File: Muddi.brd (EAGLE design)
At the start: 106.3 x 95.2 mm, 16 parts, among them IC1 7805TV, J1 DCJ0202

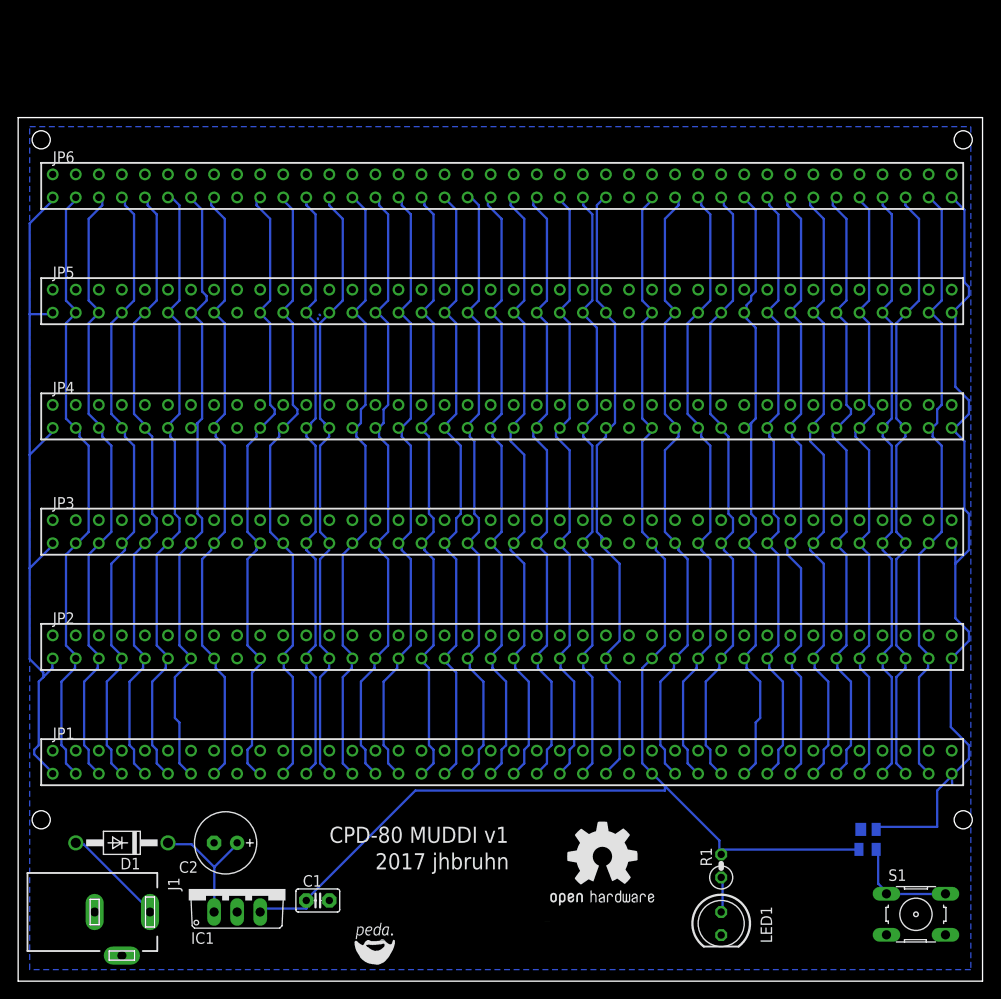
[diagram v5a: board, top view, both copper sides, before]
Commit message: Add more Texts
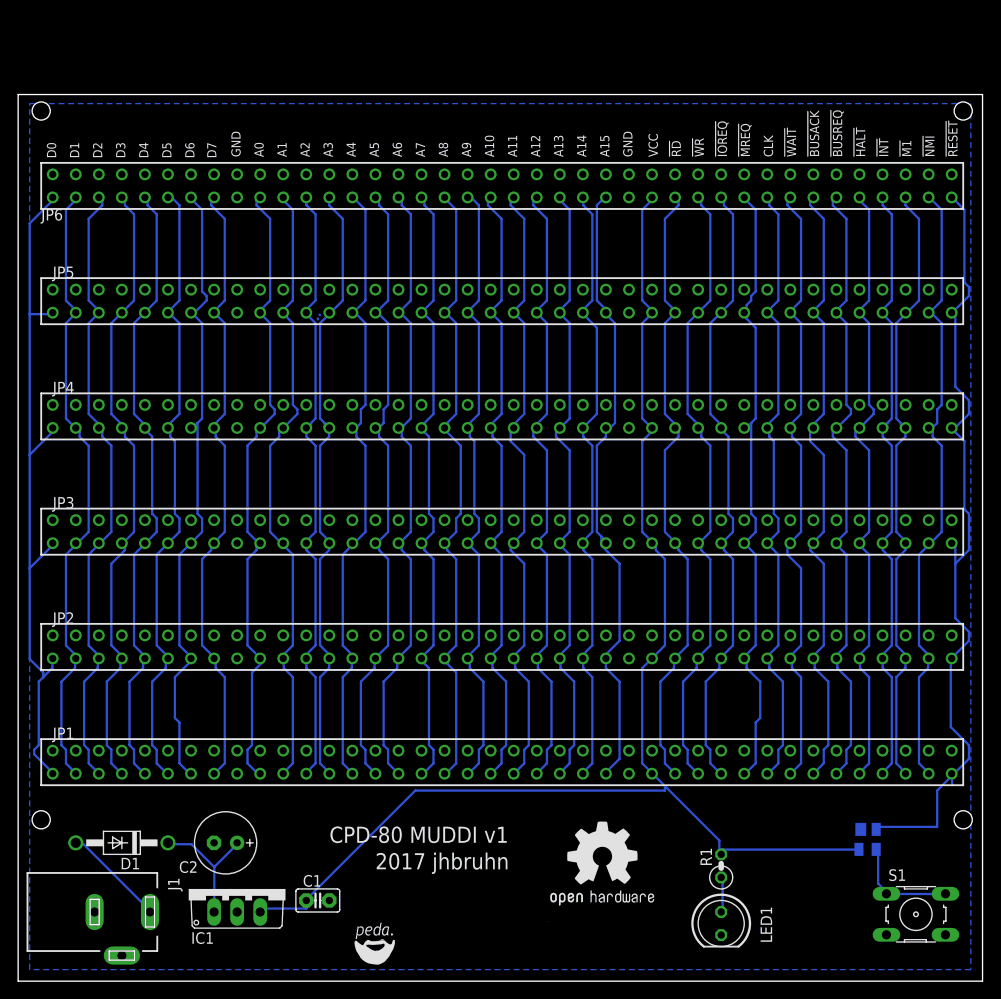
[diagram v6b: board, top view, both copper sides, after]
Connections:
- net N$1 renamed D0
- net N$24 renamed A15
- net N$37 renamed !BUSACK
- net N$38 renamed !BUSREQ
- net N$39 renamed !M1
- net N$40 renamed !RESE
- net N$41 renamed !HALT
- net N$42 renamed !NMI
- net N$43 renamed !INT
- net N$44 renamed CLK
- net N$45 renamed !MREQ
- net N$46 renamed !IOREQ
- net N$47 renamed !WAIT
- net N$48 renamed !RD
- net N$49 renamed !WR
- net N$8 renamed D7
- net N$9 renamed A0
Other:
- board size 106.3 x 95.2 mm -> 106.3 x 97.7 mm
- board text added: "!BUSACK"
- board text added: "!BUSREQ"
- board text added: "!HALT"
- board text added: "!INT"
- board text added: "!IOREQ"
- board text added: "!M1"
- board text added: "!MREQ"
- board text added: "!NMI"
- board text added: "!RD"
- board text added: "!RESET"
- board text added: "!WAIT"
- board text added: "!WR"
- board text added: "A0"
- board text added: "A1"
- board text added: "A10"
- board text added: "A11"
- board text added: "A12"
- board text added: "A13"
- board text added: "A14"
- board text added: "A15"
- board text added: "A2"
- board text added: "A3"
- board text added: "A4"
- board text added: "A5"
- board text added: "A6"
- board text added: "A7"
- board text added: "A8"
- board text added: "A9"
- board text added: "CLK"
- board text added: "D0"
- board text added: "D1"
- board text added: "D2"
- board text added: "D3"
- board text added: "D4"
- board text added: "D5"
- board text added: "D6"
- board text added: "D7"
- board text added: "GND"
- board text added: "VCC"
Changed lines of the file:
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@@
 <setting verticaltext="up"/>
 </settings>
-<grid distance="0.05" unitdist="inch" unit="mm" style="lines" multiple="1" display="no" altdistance="0.005" altunitdist="inch" altunit="mm"/>
+<grid distance="0.05" unitdist="inch" unit="mm" style="lines" multiple="1" display="no" altdistance="0.635" altunitdist="mm" altunit="mm"/>
 <layers>
 <layer number="1" name="Top" color="4" fill="1" visible="yes" active="yes"/>
@@
 <plain>
 <wire x1="-1.27" y1="0" x2="105" y2="0" width="0" layer="20"/>
-<wire x1="105" y1="0" x2="105" y2="95.16" width="0" layer="20"/>
-<wire x1="105" y1="95.16" x2="-1.27" y2="95.16" width="0" layer="20"/>
-<wire x1="-1.27" y1="95.16" x2="-1.27" y2="0" width="0" layer="20"/>
+<wire x1="105" y1="0" x2="105" y2="97.7" width="0" layer="20"/>
+<wire x1="105" y1="97.7" x2="-1.27" y2="97.7" width="0" layer="20"/>
+<wire x1="-1.27" y1="97.7" x2="-1.27" y2="0" width="0" layer="20"/>
 <text x="33.02" y="15.24" size="1.778" layer="21" font="fixed">CPD-80 MUDDI v1</text>
 <rectangle x1="38.1381" y1="1.8161" x2="38.4683" y2="1.8415" layer="21"/>
@@
 <hole x="1.27" y="17.78" drill="2"/>
 <hole x="102.87" y="17.78" drill="2"/>
-<hole x="1.27" y="92.71" drill="2"/>
-<hole x="102.87" y="92.71" drill="2"/>
+<hole x="1.27" y="95.885" drill="2"/>
+<hole x="102.87" y="95.885" drill="2"/>
+<text x="2.921" y="90.678" size="1.016" layer="21" font="fixed" rot="R90">D0</text>
+<text x="20.574" y="90.678" size="1.016" layer="21" font="fixed" rot="R90">D7</text>
+<text x="25.781" y="90.805" size="1.016" layer="21" font="fixed" rot="R90">A0</text>
+<text x="23.241" y="90.805" size="1.016" layer="21" font="fixed" rot="R90">GND</text>
+<text x="63.881" y="90.805" size="1.016" layer="21" font="fixed" rot="R90">A15</text>
+<text x="66.421" y="90.805" size="1.016" layer="21" font="fixed" rot="R90">GND</text>
+<text x="69.215" y="90.805" size="1.016" layer="21" font="fixed" rot="R90">VCC</text>
+<text x="71.755" y="90.805" size="1.016" layer="21" font="fixed" rot="R90">!RD</text>
+<text x="74.295" y="90.805" size="1.016" layer="21" font="fixed" rot="R90">!WR</text>
+<text x="76.835" y="90.805" size="1.016" layer="21" font="fixed" rot="R90">!IOREQ</text>
+<text x="79.375" y="90.805" size="1.016" layer="21" font="fixed" rot="R90">!MREQ</text>
+<text x="81.915" y="90.805" size="1.016" layer="21" font="fixed" rot="R90">CLK</text>
+<text x="84.455" y="90.805" size="1.016" layer="21" font="fixed" rot="R90">!WAIT</text>
+<text x="86.995" y="90.805" size="1.016" layer="21" font="fixed" rot="R90">!BUSACK</text>
+<text x="89.535" y="90.805" size="1.016" layer="21" font="fixed" rot="R90">!BUSREQ</text>
+<text x="92.075" y="90.805" size="1.016" layer="21" font="fixed" rot="R90">!HALT</text>
+<text x="94.615" y="90.805" size="1.016" layer="21" font="fixed" rot="R90">!INT</text>
+<text x="97.155" y="90.805" size="1.016" layer="21" font="fixed" rot="R90">!M1</text>
+<text x="99.695" y="90.805" size="1.016" layer="21" font="fixed" rot="R90">!NMI</text>
+<text x="102.235" y="90.805" size="1.016" layer="21" font="fixed" rot="R90">!RESET</text>
+<text x="5.461" y="90.678" size="1.016" layer="21" font="fixed" rot="R90">D1</text>
+<text x="8.001" y="90.678" size="1.016" layer="21" font="fixed" rot="R90">D2</text>
+<text x="10.541" y="90.678" size="1.016" layer="21" font="fixed" rot="R90">D3</text>
+<text x="13.081" y="90.678" size="1.016" layer="21" font="fixed" rot="R90">D4</text>
+<text x="15.621" y="90.678" size="1.016" layer="21" font="fixed" rot="R90">D5</text>
+<text x="18.161" y="90.678" size="1.016" layer="21" font="fixed" rot="R90">D6</text>
+<text x="28.321" y="90.805" size="1.016" layer="21" font="fixed" rot="R90">A1</text>
+<text x="30.861" y="90.805" size="1.016" layer="21" font="fixed" rot="R90">A2</text>
+<text x="33.401" y="90.805" size="1.016" layer="21" font="fixed" rot="R90">A3</text>
+<text x="35.941" y="90.805" size="1.016" layer="21" font="fixed" rot="R90">A4</text>
+<text x="38.481" y="90.805" size="1.016" layer="21" font="fixed" rot="R90">A5</text>
+<text x="41.021" y="90.805" size="1.016" layer="21" font="fixed" rot="R90">A6</text>
+<text x="43.561" y="90.805" size="1.016" layer="21" font="fixed" rot="R90">A7</text>
+<text x="46.101" y="90.805" size="1.016" layer="21" font="fixed" rot="R90">A8</text>
+<text x="48.641" y="90.805" size="1.016" layer="21" font="fixed" rot="R90">A9</text>
+<text x="51.181" y="90.805" size="1.016" layer="21" font="fixed" rot="R90">A10</text>
+<text x="53.721" y="90.805" size="1.016" layer="21" font="fixed" rot="R90">A11</text>
+<text x="56.261" y="90.805" size="1.016" layer="21" font="fixed" rot="R90">A12</text>
+<text x="58.801" y="90.805" size="1.016" layer="21" font="fixed" rot="R90">A13</text>
+<text x="61.341" y="90.805" size="1.016" layer="21" font="fixed" rot="R90">A14</text>
 </plain>
 <attributes>
@@
 <element name="JP4" library="jean" package="57102-F08-25" value="" x="11.43" y="62.23"/>
 <element name="JP5" library="jean" package="57102-F08-25" value="" x="11.43" y="74.93"/>
-<element name="JP6" library="jean" package="57102-F08-25" value="" x="11.43" y="87.63"/>
+<element name="JP6" library="jean" package="57102-F08-25" value="" x="11.43" y="87.63" smashed="yes">
+<attribute name="NAME" x="1.27" y="83.82" size="1.27" layer="25"/>
+<attribute name="VALUE" x="2.54" y="83.185" size="1.27" layer="27"/>
+</element>
 <element name="S1" library="switch-omron" package="B3F-10XX" value="RESET" x="97.663" y="7.366">
 <attribute name="OC_FARNELL" value="176432" x="97.663" y="7.366" size="1.778" layer="27" display="off"/>
@@
 </elements>
 <signals>
-<signal name="N$1">
+<signal name="D0">
 <contactref element="JP1" pad="1"/>
 <contactref element="JP2" pad="1"/>
@@
 <wire x1="18" y1="48.5" x2="17.78" y2="48.26" width="0.254" layer="16"/>
 </signal>
-<signal name="N$8">
+<signal name="D7">
 <contactref element="JP6" pad="15"/>
 <contactref element="JP5" pad="15"/>
@@
 <wire x1="20.5" y1="61" x2="20.32" y2="60.96" width="0.254" layer="16"/>
 </signal>
-<signal name="N$9">
+<signal name="A0">
 <contactref element="JP1" pad="19"/>
 <contactref element="JP2" pad="19"/>
@@
 <wire x1="61" y1="73.5" x2="60.96" y2="73.66" width="0.254" layer="16"/>
 </signal>
-<signal name="N$24">
+<signal name="A15">
 <contactref element="JP2" pad="49"/>
 <contactref element="JP1" pad="49"/>
@@
 <wire x1="63.5" y1="60.5" x2="63.5" y2="60.96" width="0.254" layer="16"/>
 </signal>
-<signal name="N$37">
+<signal name="!BUSACK">
 <contactref element="JP2" pad="67"/>
 <contactref element="JP1" pad="67"/>
@@
 <wire x1="86.5" y1="61" x2="86.36" y2="60.96" width="0.254" layer="16"/>
 </signal>
-<signal name="N$38">
+<signal name="!BUSREQ">
 <contactref element="JP1" pad="69"/>
 <contactref element="JP2" pad="69"/>
@@
 <wire x1="89" y1="61" x2="88.9" y2="60.96" width="0.254" layer="16"/>
 </signal>
-<signal name="N$39">
+<signal name="!M1">
 <contactref element="JP2" pad="75"/>
 <contactref element="JP1" pad="75"/>
@@
 <wire x1="96.5" y1="60.5" x2="96.52" y2="60.96" width="0.254" layer="16"/>
 </signal>
-<signal name="N$40">
+<signal name="!RESE">
 <contactref element="JP1" pad="79"/>
 <contactref element="JP2" pad="79"/>
@@
 <wire x1="102" y1="60.5" x2="101.6" y2="60.96" width="0.254" layer="16"/>
 </signal>
-<signal name="N$41">
+<signal name="!HALT">
 <contactref element="JP2" pad="71"/>
 <contactref element="JP1" pad="71"/>
@@
 <wire x1="91.5" y1="61" x2="91.44" y2="60.96" width="0.254" layer="16"/>
 </signal>
-<signal name="N$42">
+<signal name="!NMI">
 <contactref element="JP1" pad="77"/>
 <contactref element="JP2" pad="77"/>
@@
 <wire x1="99.5" y1="61" x2="99.06" y2="60.96" width="0.254" layer="16"/>
 </signal>
-<signal name="N$43">
+<signal name="!INT">
 <contactref element="JP2" pad="73"/>
 <contactref element="JP1" pad="73"/>
@@
 <wire x1="94" y1="60.5" x2="93.98" y2="60.96" width="0.254" layer="16"/>
 </signal>
-<signal name="N$44">
+<signal name="CLK">
 <contactref element="JP1" pad="63"/>
 <contactref element="JP2" pad="63"/>
@@
 <wire x1="81.5" y1="61" x2="81.28" y2="60.96" width="0.254" layer="16"/>
 </signal>
-<signal name="N$45">
+<signal name="!MREQ">
 <contactref element="JP2" pad="61"/>
 <contactref element="JP1" pad="61"/>
@@
 <wire x1="79" y1="48.5" x2="78.74" y2="48.26" width="0.254" layer="16"/>
 </signal>
-<signal name="N$46">
+<signal name="!IOREQ">
 <contactref element="JP1" pad="59"/>
 <contactref element="JP2" pad="59"/>
@@
 <wire x1="76" y1="61" x2="76.2" y2="60.96" width="0.254" layer="16"/>
 </signal>
-<signal name="N$47">
+<signal name="!WAIT">
 <contactref element="JP2" pad="65"/>
 <contactref element="JP1" pad="65"/>
@@
 <wire x1="84" y1="61" x2="83.82" y2="60.96" width="0.254" layer="16"/>
 </signal>
-<signal name="N$48">
+<signal name="!RD">
 <contactref element="JP1" pad="55"/>
 <contactref element="JP2" pad="55"/>
@@
 <wire x1="71" y1="61" x2="71.12" y2="60.96" width="0.254" layer="16"/>
 </signal>
-<signal name="N$49">
+<signal name="!WR">
 <contactref element="JP2" pad="57"/>
 <contactref element="JP1" pad="57"/>
@@
 <contactref element="JP6" pad="51"/>
 <polygon width="0.254" layer="16" isolate="0.3048">
-<vertex x="0" y="94.16"/>
-<vertex x="103.7082" y="94.16"/>
+<vertex x="0" y="96.7"/>
+<vertex x="103.7082" y="96.7"/>
 <vertex x="103.7082" y="1.27"/>
 <vertex x="0" y="1.27"/>

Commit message: Fix stupid VCC/GND mistakes on Address decoder
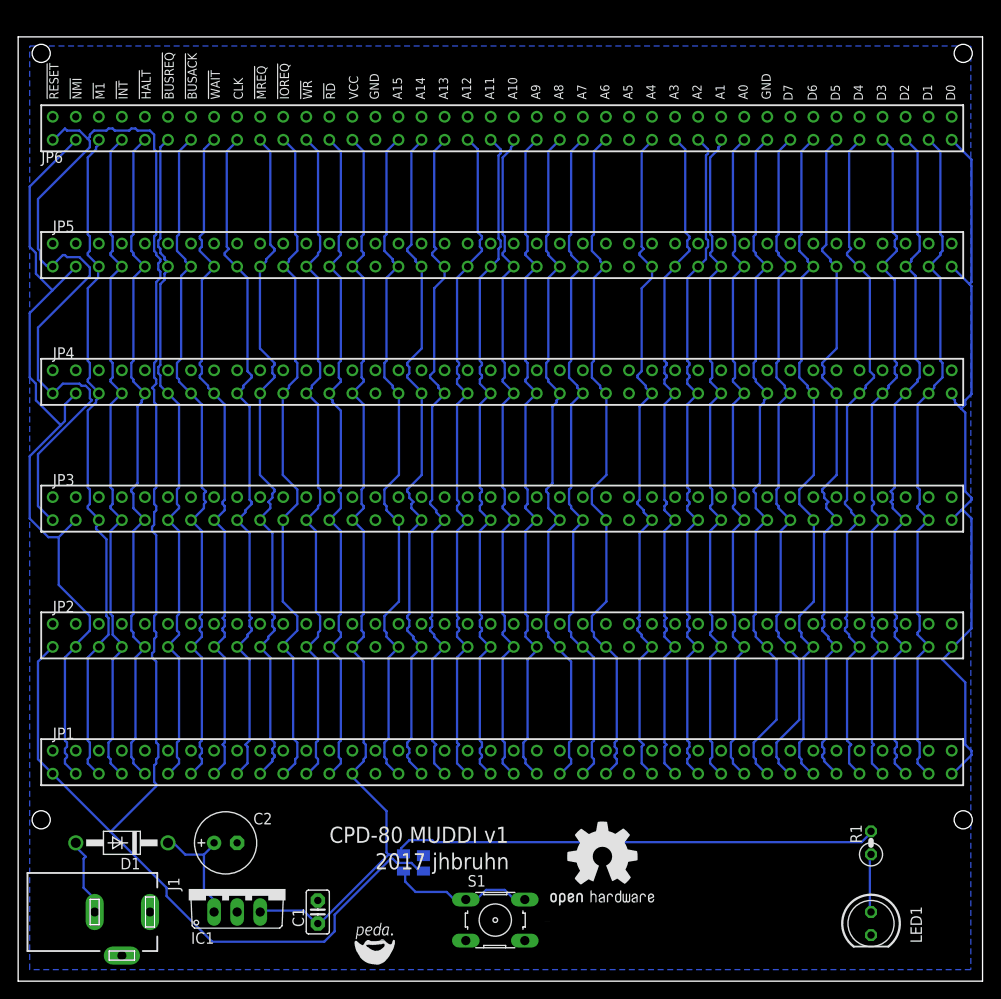
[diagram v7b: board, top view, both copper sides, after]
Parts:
- moved MAX811 50.1 mm to (42.3, 13.1), turned to 270 degrees
- moved S1 46.4 mm to (51.3, 6.73)
- moved R1 16.7 mm to (92.7, 15.2)
- moved LED1 16.5 mm to (92.7, 6.35)
- moved JP6 6.35 mm to (11.4, 94.0)
- moved JP5 5.08 mm to (11.4, 80.0)
- moved JP4 3.81 mm to (11.4, 66.0)
- moved JP3 2.54 mm to (11.4, 52.1)
- moved JP2 1.27 mm to (11.4, 38.1)
- moved C1 1.27 mm to (31.8, 7.62), turned to 90 degrees
- turned C2 to 0 degrees
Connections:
- removed net N$28: D1.A, J1.1
- new net N$1: D1.A, J1.3
- net !BUSACK: now also JP1.13, JP2.13, JP3.13, JP4.13, JP5.13, JP6.13; no longer JP1.67, JP2.67, JP3.67, JP4.67, JP5.67, JP6.67
- net !BUSREQ: now also JP1.11, JP2.11, JP3.11, JP4.11, JP5.11, JP6.11; no longer JP1.69, JP2.69, JP3.69, JP4.69, JP5.69, JP6.69
- net !HALT: now also JP1.9, JP2.9, JP3.9, JP4.9, JP5.9, JP6.9; no longer JP1.71, JP2.71, JP3.71, JP4.71, JP5.71, JP6.71
- net !INT: now also JP1.7, JP2.7, JP3.7, JP4.7, JP5.7, JP6.7; no longer JP1.73, JP2.73, JP3.73, JP4.73, JP5.73, JP6.73
- net !IOREQ: now also JP1.21, JP2.21, JP3.21, JP4.21, JP5.21, JP6.21; no longer JP1.59, JP2.59, JP3.59, JP4.59, JP5.59, JP6.59
- net !M1: now also JP1.5, JP2.5, JP3.5, JP4.5, JP5.5, JP6.5; no longer JP1.75, JP2.75, JP3.75, JP4.75, JP5.75, JP6.75
- net !MREQ: now also JP1.19, JP2.19, JP3.19, JP4.19, JP5.19, JP6.19; no longer JP1.61, JP2.61, JP3.61, JP4.61, JP5.61, JP6.61
- net !NMI: now also JP1.3, JP2.3, JP3.3, JP4.3, JP5.3, JP6.3; no longer JP1.77, JP2.77, JP3.77, JP4.77, JP5.77, JP6.77
- net !RD: now also JP1.25, JP2.25, JP3.25, JP4.25, JP5.25, JP6.25; no longer JP1.55, JP2.55, JP3.55, JP4.55, JP5.55, JP6.55
- net !RESE: now also JP1.1, JP2.1, JP3.1, JP4.1, JP5.1, JP6.1; no longer JP1.79, JP2.79, JP3.79, JP4.79, JP5.79, JP6.79
- net !WAIT: now also JP1.15, JP2.15, JP3.15, JP4.15, JP5.15, JP6.15; no longer JP1.65, JP2.65, JP3.65, JP4.65, JP5.65, JP6.65
- net !WR: now also JP1.23, JP2.23, JP3.23, JP4.23, JP5.23, JP6.23; no longer JP1.57, JP2.57, JP3.57, JP4.57, JP5.57, JP6.57
- net A0: now also JP1.63, JP2.63, JP3.63, JP4.63, JP5.63, JP6.63; no longer JP1.19, JP2.19, JP3.19, JP4.19, JP5.19, JP6.19
- net A15: now also JP1.31, JP2.31, JP3.31, JP4.31, JP5.31, JP6.31; no longer JP1.49, JP2.49, JP3.49, JP4.49, JP5.49, JP6.49
- net CLK: now also JP1.17, JP2.17, JP3.17, JP4.17, JP5.17, JP6.17; no longer JP1.63, JP2.63, JP3.63, JP4.63, JP5.63, JP6.63
- net D0: now also JP1.79, JP2.79, JP3.79, JP4.79, JP5.79, JP6.79; no longer JP1.1, JP2.1, JP3.1, JP4.1, JP5.1, JP6.1
- net D7: now also JP1.65, JP2.65, JP3.65, JP4.65, JP5.65, JP6.65; no longer JP1.15, JP2.15, JP3.15, JP4.15, JP5.15, JP6.15
- net GND: now also J1.1, JP1.29, JP2.29, JP3.29, JP4.29, JP5.29, JP6.29; no longer J1.3, JP1.17, JP2.17, JP3.17, JP4.17, JP5.17, JP6.17
- net N$10: now also JP1.61, JP2.61, JP3.61, JP4.61, JP5.61, JP6.61; no longer JP1.21, JP2.21, JP3.21, JP4.21, JP5.21, JP6.21
- net N$11: now also JP1.59, JP2.59, JP3.59, JP4.59, JP5.59, JP6.59; no longer JP1.23, JP2.23, JP3.23, JP4.23, JP5.23, JP6.23
- net N$12: now also JP1.57, JP2.57, JP3.57, JP4.57, JP5.57, JP6.57; no longer JP1.25, JP2.25, JP3.25, JP4.25, JP5.25, JP6.25
- net N$13: now also JP1.55, JP2.55, JP3.55, JP4.55, JP5.55, JP6.55; no longer JP1.27, JP2.27, JP3.27, JP4.27, JP5.27, JP6.27
- net N$14: now also JP1.53, JP2.53, JP3.53, JP4.53, JP5.53, JP6.53; no longer JP1.29, JP2.29, JP3.29, JP4.29, JP5.29, JP6.29
- net N$15: now also JP1.49, JP2.49, JP3.49, JP4.49, JP5.49, JP6.49; no longer JP1.31, JP2.31, JP3.31, JP4.31, JP5.31, JP6.31
- net N$2: now also JP1.77, JP2.77, JP3.77, JP4.77, JP5.77, JP6.77; no longer JP1.3, JP2.3, JP3.3, JP4.3, JP5.3, JP6.3
- net N$3: now also JP1.75, JP2.75, JP3.75, JP4.75, JP5.75, JP6.75; no longer JP1.5, JP2.5, JP3.5, JP4.5, JP5.5, JP6.5
- net N$4: now also JP1.73, JP2.73, JP3.73, JP4.73, JP5.73, JP6.73; no longer JP1.7, JP2.7, JP3.7, JP4.7, JP5.7, JP6.7
- net N$5: now also JP1.71, JP2.71, JP3.71, JP4.71, JP5.71, JP6.71; no longer JP1.9, JP2.9, JP3.9, JP4.9, JP5.9, JP6.9
- net N$6: now also JP1.69, JP2.69, JP3.69, JP4.69, JP5.69, JP6.69; no longer JP1.11, JP2.11, JP3.11, JP4.11, JP5.11, JP6.11
- net N$7: now also JP1.67, JP2.67, JP3.67, JP4.67, JP5.67, JP6.67; no longer JP1.13, JP2.13, JP3.13, JP4.13, JP5.13, JP6.13
- net VCC: now also JP1.27, JP2.27, JP3.27, JP4.27, JP5.27, JP6.27; no longer JP1.53, JP2.53, JP3.53, JP4.53, JP5.53, JP6.53
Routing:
- net !RESE: track 88.6 -> 227.6 mm
- net !NMI: track 69.3 -> 92.8 mm
- net VCC: track 147.7 -> 160.6 mm
- net N$28: track 11.4 -> 0.00 mm
- net D7: track 68.8 -> 78.0 mm
- net N$16: track 68.1 -> 77.1 mm
- net N$1: track 0.00 -> 8.67 mm
- net N$3: track 69.1 -> 77.6 mm
- net N$23: track 69.4 -> 77.7 mm
- net N$12: track 68.6 -> 76.7 mm
- net !IOREQ: track 69.3 -> 77.4 mm
- net !MREQ: track 69.6 -> 77.7 mm
- net N$6: track 69.6 -> 77.7 mm
- net !BUSACK: track 69.5 -> 77.6 mm
- net !WAIT: track 68.9 -> 77.0 mm
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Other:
- board size 106.3 x 97.7 mm -> 106.3 x 104 mm
